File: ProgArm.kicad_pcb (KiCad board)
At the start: 2 copper layers, 40 x 50 mm, 130 parts, among them M1 MOTOR, P1 I²C_Port, P10 TXD, P11 RING_VCC, P12 RING_GND, P13 RING_GPIOA_3_Port, P14 RING_GPIOA_4_Port, P15 RXD, P16 RING_BUTTONS_Port, P17 MicroUSB, P2 SPI_Port, P3 UART_Port, P4 SWD_Port, P5 GPIOA_1_2_Port, P6 TIM1_Port, P7 T_SENS, P8 RING_IR_OUT, P9 RING_LEDS_Port, Q1 MOS_P, Q2 MOS_P, Q3 MOS_P, Q4 MOS_P, Q5 MOS_P, Q6 MOS_P, Q7 MOS_P, Q8 MOS_P, SW1 FW/RST, SW2 ON/OFF, U1 TPS78330, U2 BQ24297, U3 LM3668, U4 STM32F103R, U5 MPU9250, U6 BQ27410, U7 SI1143, U8 LPS25H, U9 NRF8001, X1 32.768kHz, X2 8MHz, X3 16MHz

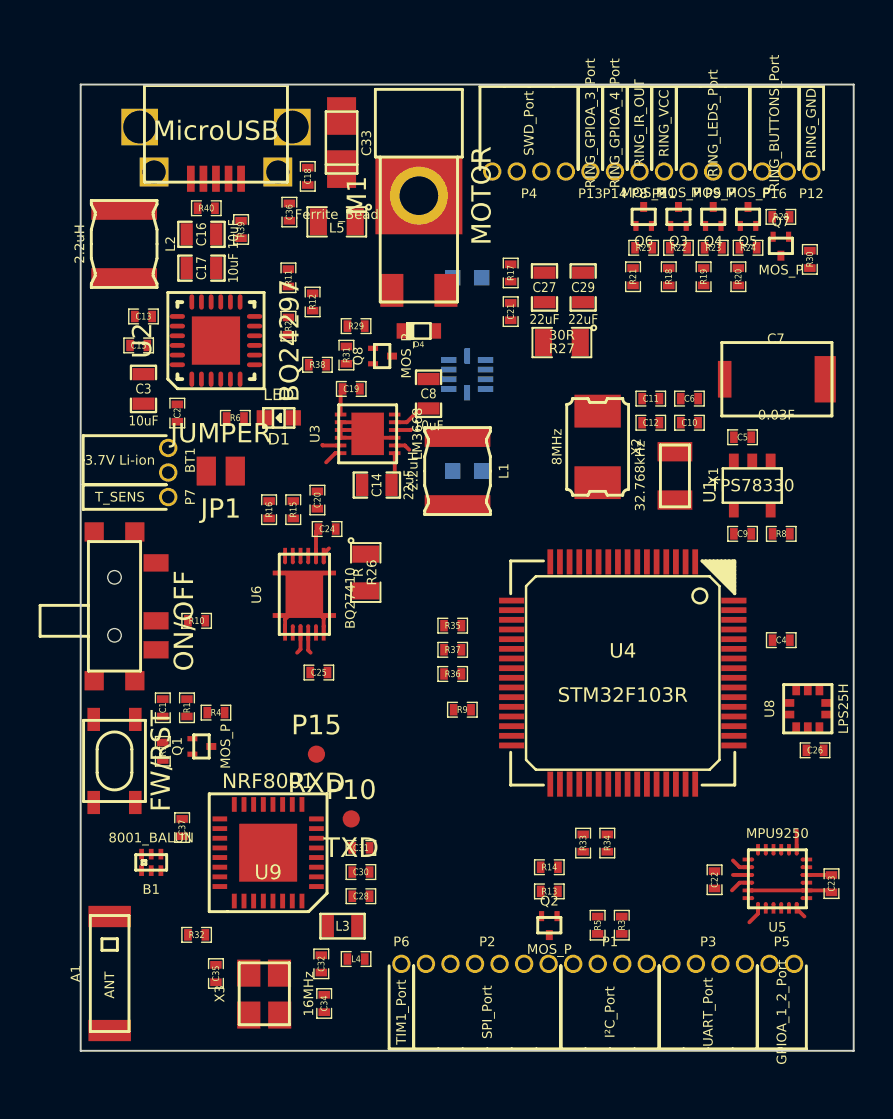
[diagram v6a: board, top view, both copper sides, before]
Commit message: Small fixes for proper power tracks
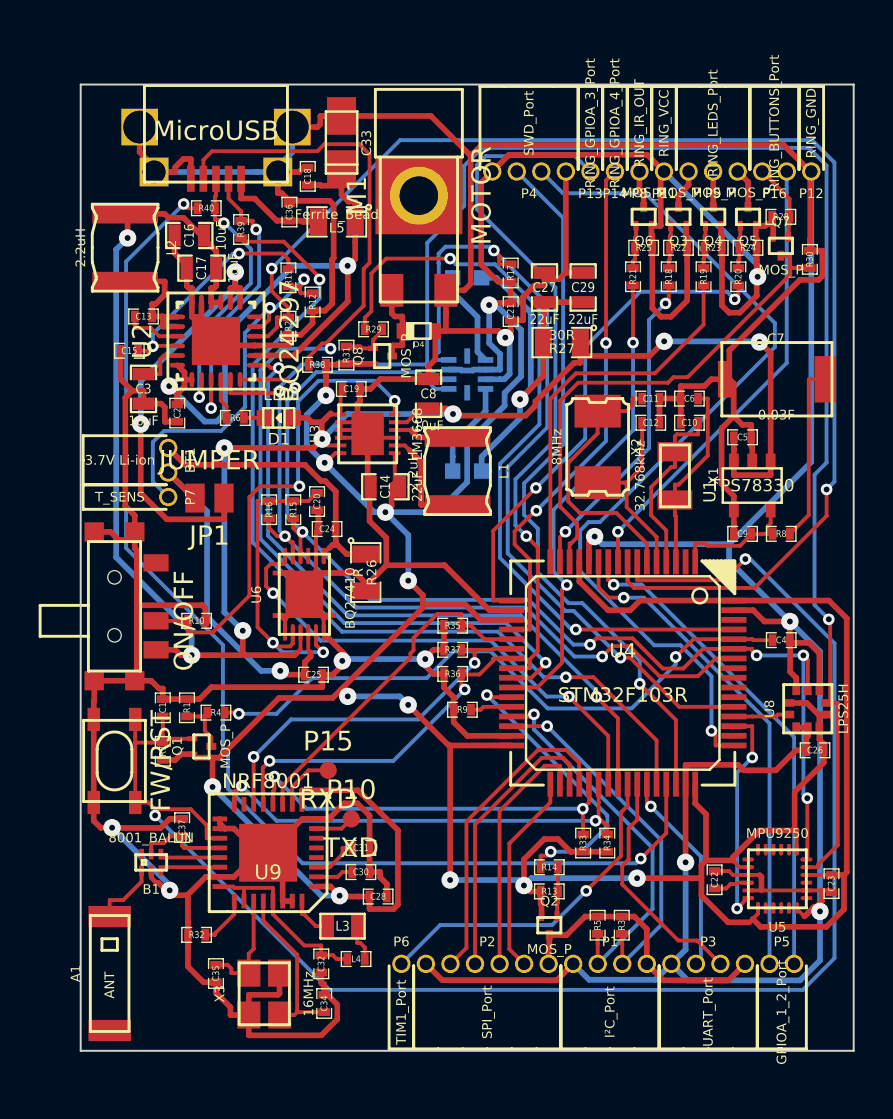
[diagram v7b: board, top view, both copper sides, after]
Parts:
- moved JP1 1.52 mm to (51.7, 66.4)
- moved P15 1.03 mm to (57.8, 80.5)
- moved R29 0.92 mm to (60.2, 57.7)
- moved C28 0.89 mm to (60.4, 87.0)
- moved C16 0.63 mm to (50.6, 52.8)
- moved C15 0.56 mm to (47.5, 58.8)
- moved C14 0.45 mm to (60.8, 65.8)
- moved C25 0.30 mm to (57.1, 75.5)
- moved L2 0.20 mm to (47.3, 53.4)
- moved C20 0.08 mm to (57.2, 66.6)
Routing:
- net GND: track 19.5 -> 417.4 mm, vias 0 -> 9
- net +3.3V: track 7.15 -> 249.9 mm, vias 0 -> 13
- net SCL: track 0.00 -> 120.2 mm, vias 0 -> 4
- net VCC: track 5.82 -> 105.6 mm, vias 0 -> 8
- net ~RESET: track 0.00 -> 83.7 mm, vias 0 -> 2
- net IN_CURRENT: track 0.00 -> 69.2 mm, vias 0 -> 2
- net SDA: track 0.00 -> 64.8 mm, vias 0 -> 6
- net D+: track 0.00 -> 61.9 mm, vias 0 -> 2
- net ~OTG_cable: track 0.00 -> 55.2 mm, vias 0 -> 2
- net D-: track 0.00 -> 47.5 mm, vias 0 -> 2
- net SWCLK: track 0.00 -> 46.4 mm, vias 0 -> 1
- net ~SI_INT: track 0.00 -> 43.4 mm, vias 0 -> 2
- net ~VIBRATION: track 0.00 -> 40.5 mm, vias 0 -> 2
- net SWDIO: track 0.00 -> 37.2 mm, vias 0 -> 1
- net GPIOA_3: track 0.00 -> 36.6 mm, vias 0 -> 1
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
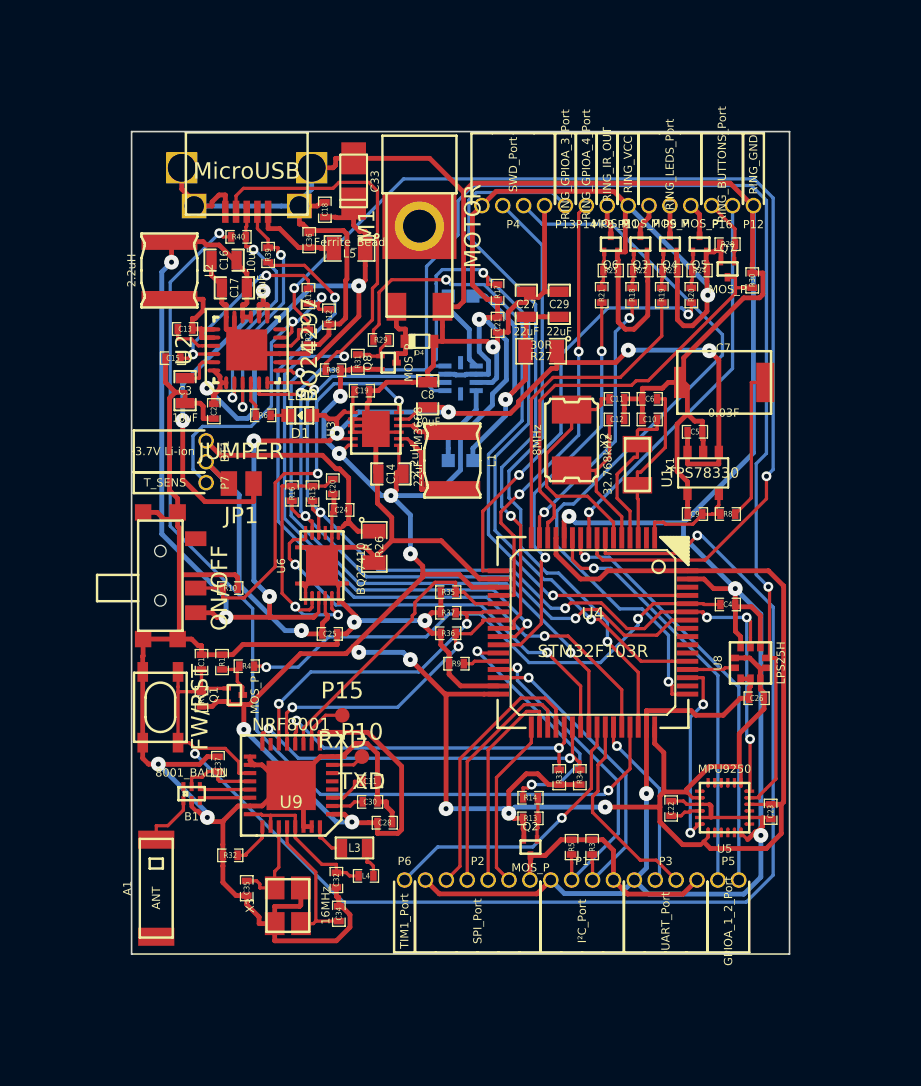
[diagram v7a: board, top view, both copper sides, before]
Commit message: Wide traces, pours
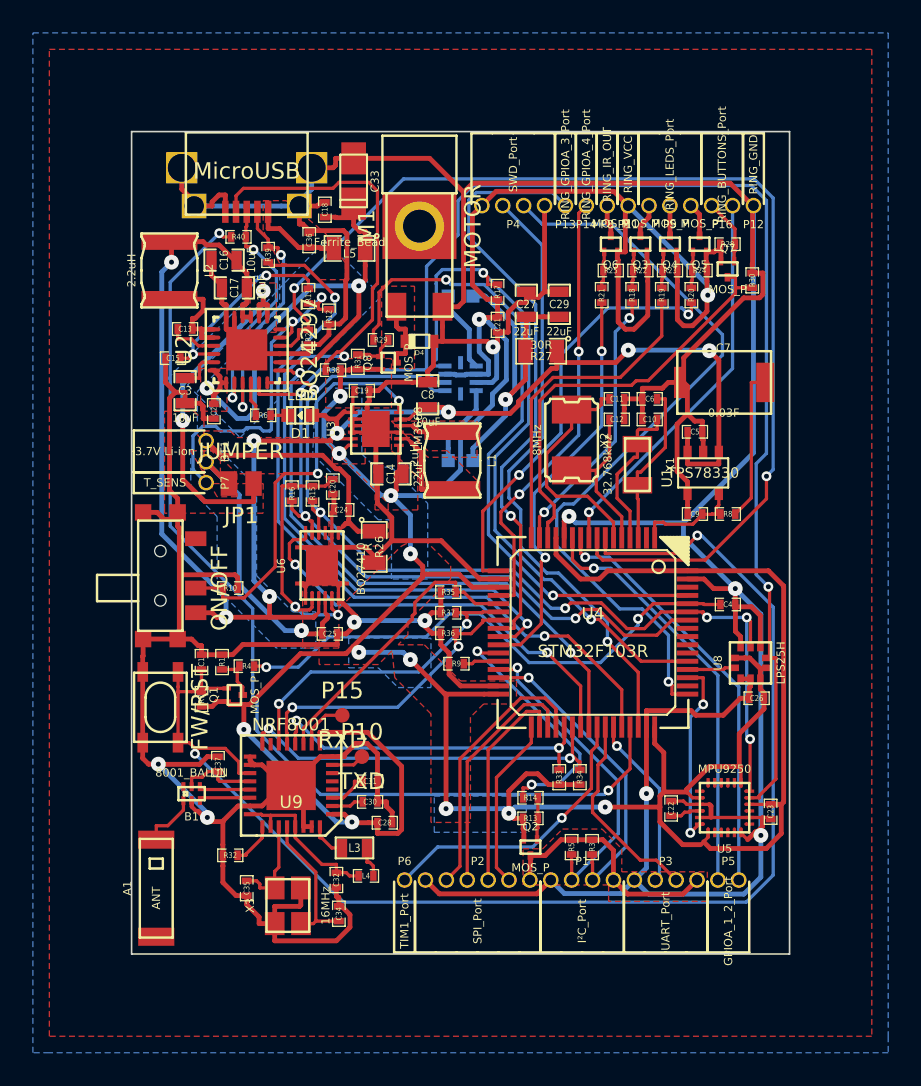
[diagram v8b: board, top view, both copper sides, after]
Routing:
- net N-000009: track 20.3 -> 21.5 mm
- added copper zone on B.Cu, net +3.3V
- added copper zone on F.Cu, net +3.3V
- added copper zone on B.Cu, net +5V
- added copper zone on F.Cu, net +5V
- added copper zone on B.Cu, net BATTERY
- added copper zone on F.Cu, net BATTERY
- added copper zone on B.Cu, net GND
- added copper zone on F.Cu, net GND
- added copper zone on F.Cu, net N-00000102
- added copper zone on B.Cu, net N-00000107
- added copper zone on F.Cu, net N-00000107
- added copper zone on F.Cu, net N-0000027
- added copper zone on F.Cu, net N-0000034
- added copper zone on F.Cu, net N-0000035
- added copper zone on F.Cu, net N-0000088
- added copper zone on F.Cu, net PORT_POWER
